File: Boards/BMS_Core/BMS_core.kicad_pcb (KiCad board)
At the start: 2 copper layers, 73.7 x 61 mm, 72 parts, among them IC1 ATMEGA16M1, J1 CONN_02X03, J2 B5B-PH-K-S, J3 MM_F_VT_20, J4 MicroFit_V_2, J5 isoSPI-Cutout, K1 G5Q-1A4-DC5-5V, Q1 SSM3K333R, T1 T_LAN_7490100111A, U1 MCP2561-E_SN, U101 TPS561201, U2 SN74LVC1G17, U3 LTC6820HMS, U4 MCP6001, U5 MCP6001, U6 MCP6001, U7 SN74LVC1G32, Y1 Crystal_SMD

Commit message: update BMS Core schemtic)
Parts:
- moved C6 71.3 mm to (115.9, 32.4), turned to 0 degrees
- moved T1 70.1 mm to (68.0, 41.0), turned to 0 degrees
- moved C9 69.1 mm to (108.4, 37.4), turned to 0 degrees
- moved R11 65.0 mm to (114.2, 42.2)
- moved C8 62.0 mm to (101.6, 45.8), turned to 0 degrees
- moved R3 59.2 mm to (105.9, 43.1), turned to 0 degrees
- moved U3 57.3 mm to (102.5, 38.8), turned to 0 degrees
- moved R8 56.8 mm to (110.1, 45.9), turned to 0 degrees
- moved R9 54.6 mm to (105.2, 48.8), turned to 0 degrees
- moved R10 54.1 mm to (102.2, 53.2), turned to 0 degrees
- moved U2 51.9 mm to (96.9, 43.9)
- moved J4 50.4 mm to (94.2, 37.6)
- moved Y1 47.9 mm to (111.3, 28.5)
- moved C1 46.9 mm to (113.0, 36.4)
- moved C10 46.6 mm to (120.8, 27.7)
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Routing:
- net VCC: track 240.5 -> 20.5 mm, vias 7 -> 1
- net /VOUT: track 81.1 -> 0.00 mm, vias 2 -> 0
- net /BSPD_CURRENT: track 79.8 -> 0.00 mm, vias 4 -> 0
- net /MISO: track 73.4 -> 0.00 mm, vias 3 -> 0
- net /VREF: track 72.7 -> 0.00 mm, vias 6 -> 0
- net /RESET: track 70.9 -> 0.00 mm, vias 4 -> 0
- net /MOSI: track 69.8 -> 0.00 mm, vias 3 -> 0
- net /SCK: track 64.6 -> 0.00 mm, vias 5 -> 0
- net GND: track 68.3 -> 14.4 mm, vias 46 -> 14
- net /RXCAN: track 42.6 -> 0.00 mm
- net /BMS_SENSE: track 40.0 -> 0.00 mm, vias 2 -> 0
- net /~OCD: track 39.7 -> 0.00 mm, vias 2 -> 0
- net +12V: track 55.5 -> 17.0 mm
- net /RJ45_LED2: track 37.1 -> 0.00 mm, vias 2 -> 0
- net /FAN_PWM_RAW: track 35.6 -> 2.57 mm, vias 2 -> 0
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- removed copper zone on B.Cu, net GND
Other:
- board outline removed
- board text removed: "GLV"
- board text removed: "HV"
- board text removed: "IM IP"
- board text removed: "MKIV BMS Core Rev 1.4 Olin Electric Motorsports Alexander Hoppe '19 Lucky Jordan '21 5/19/19"
- board text removed: "PD5"
- board text removed: "PD6"
- board text removed: "PD7"

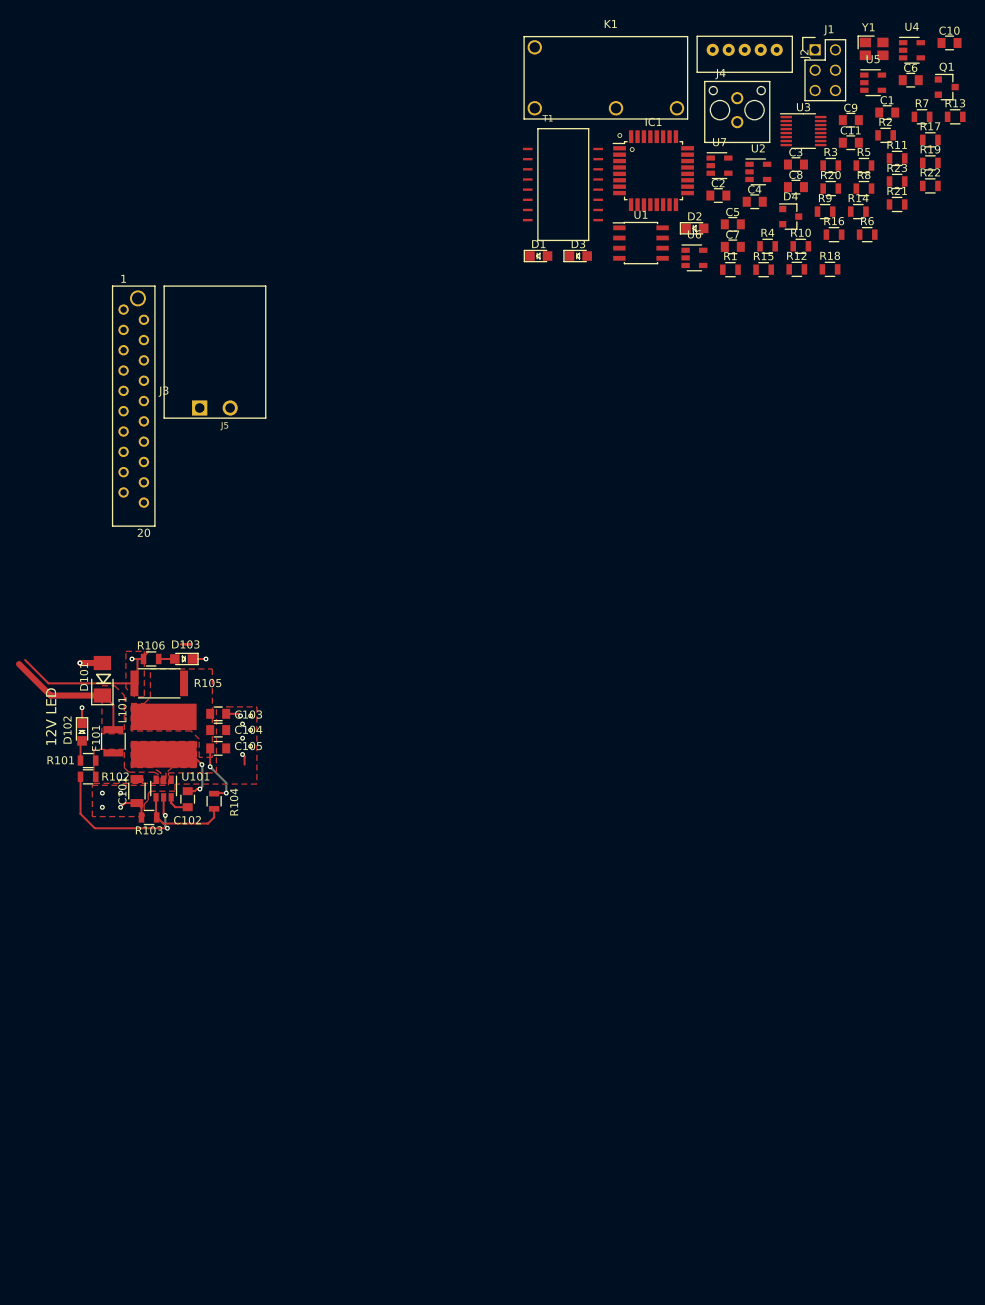
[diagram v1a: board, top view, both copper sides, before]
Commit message: Added bypass cap to Logic block; new core layout for ss layout
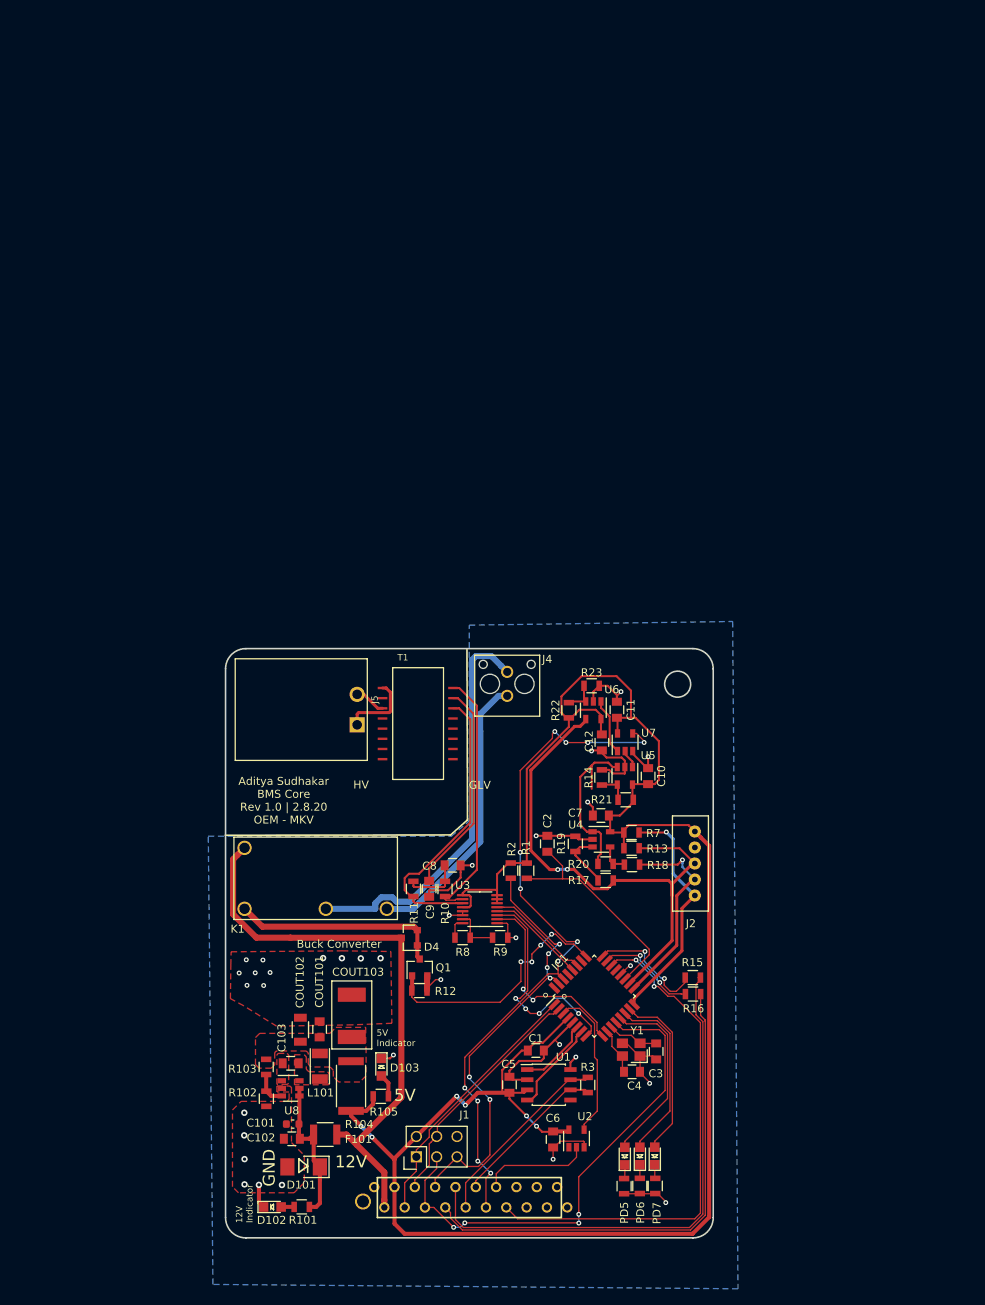
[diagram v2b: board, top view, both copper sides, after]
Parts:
- removed C104: C_1uF, footprints:C_0805_OEM
- removed C105: C_0.1uF, footprints:C_0805_OEM
- removed D1, D2, D3: LED_0805, footprints:LED_0805_OEM
- removed R106: R_200, footprints:R_0805_OEM
- removed U101: TPS561201, footprints:SOT-23-6_OEM
- added C12: C_0.1uF, footprints:C_0805_OEM, F.Cu at (77.3, 115.2)
- added COUT101: C_47uF, footprints:C_0805_OEM, F.Cu at (42.0, 151.0)
- added COUT102: C_22uF, footprints:C_1206_OEM, F.Cu at (39.6, 151.1)
- added COUT103: C_33uF, footprints:Fuse_1812, F.Cu at (46.0, 152.0)
- added PD5: LED_0805, footprints:LED_0805_OEM, F.Cu at (80.2, 166.9)
- added PD6: LED_0805, footprints:LED_0805_OEM, F.Cu at (82.0, 166.9)
- added PD7: LED_0805, footprints:LED_0805_OEM, F.Cu at (83.9, 166.9)
- added U8: TPS560430YF, footprints:SOT-23-6_OEM, F.Cu at (38.4, 158.4)
- C101: value C_22uF -> C_2.2uF; footprint footprints:C_1206_OEM -> footprints:C_0603_1608Metric
- C103: value C_47uF -> C_0.1uF
- J3: moved to B.Cu
- L101: value L_4.7uH -> L_100uH; footprint footprints:4.7uH_Inductor_OEM -> footprints:L_100uH_OEM
- R102: value R_10K -> R_25K
- R103: value R_10K -> R_100K
- R104: value R_54.9K -> R_0_2512; footprint footprints:R_0805_OEM -> footprints:R_2512_OEM
- R105: value R_0_2512 -> R_200; footprint footprints:R_2512_OEM -> footprints:R_0805_OEM
- moved J1 147.1 mm to (54.1, 167.0), turned to 90 degrees
- moved C6 139.8 mm to (71.2, 164.8), turned to 90 degrees
- moved R5 130.6 mm to (82.0, 170.6), turned to 270 degrees
- moved Y1 128.7 mm to (81.0, 153.6), turned to 180 degrees
- moved Q1 128.3 mm to (54.5, 143.3), turned to 90 degrees
- moved C1 125.2 mm to (69.0, 153.7)
- moved U2 122.9 mm to (74.1, 164.7), turned to 90 degrees
- moved R6 121.8 mm to (84.0, 170.6), turned to 270 degrees
- moved R3 118.9 mm to (75.5, 158.0), turned to 270 degrees
- moved R4 118.8 mm to (80.1, 170.6), turned to 270 degrees
- moved C3 112.2 mm to (84.1, 153.8), turned to 270 degrees
- moved C5 111.1 mm to (65.7, 158.0), turned to 90 degrees
- moved J3 110.8 mm to (53.9, 170.8), turned to 270 degrees
- moved C4 109.8 mm to (81.1, 156.3)
- moved C9 109.6 mm to (55.7, 133.5), turned to 270 degrees
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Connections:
- C102 pad 1: Net-(C102-Pad1) -> Net-(C101-Pad1)
- C102 pad 2: Net-(C102-Pad2) -> GND
- C103 pad 2: GND -> Net-(C103-Pad2)
- D101 pad 1: +12V -> Net-(C101-Pad1)
- D4 pad 2: (no net) -> Net-(D4-Pad1)
- J3 pad 15: /Charge-Enable-1 -> GND
- J3 pad 16: /Charge-Enable-2 -> GND
- J3 pad 21: (no net) -> GND
- L101 pad 1: Net-(C102-Pad2) -> Net-(C103-Pad1)
- L101 pad 2: Net-(C103-Pad1) -> Net-(COUT101-Pad1)
- R102 pad 2: Net-(C101-Pad1) -> GND
- R103 pad 1: Net-(R103-Pad1) -> Net-(R102-Pad1)
- R103 pad 2: GND -> Net-(COUT101-Pad1)
- R104 pad 1: Net-(R103-Pad1) -> VCC
- R104 pad 2: Net-(C103-Pad1) -> Net-(COUT101-Pad1)
- R105 pad 2: Net-(C103-Pad1) -> Net-(D103-Pad2)
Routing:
- net VCC: track 20.5 -> 254.8 mm, vias 1 -> 6
- net /BSPD_CURRENT: track 0.00 -> 88.9 mm, vias 0 -> 12
- net GND: track 14.4 -> 93.7 mm, vias 14 -> 28
- net /VOUT: track 0.00 -> 67.9 mm, vias 0 -> 2
- net /RJ45_LED2: track 0.00 -> 66.6 mm
- net /BMS_SENSE: track 0.00 -> 64.2 mm, vias 0 -> 2
- net /RJ45_LED1: track 0.00 -> 63.2 mm
- net /SCK: track 0.00 -> 62.2 mm, vias 0 -> 4
- net /RESET: track 0.00 -> 57.3 mm, vias 0 -> 6
- net +12V: track 17.0 -> 71.6 mm
- net /SHDN_OUT(BMS->IMD): track 0.00 -> 50.6 mm
- net Net-(R11-Pad2): track 0.00 -> 36.5 mm
- net /SHDN_IN(MAIN_PACK->BMS): track 0.00 -> 35.5 mm
- net /MISO: track 0.00 -> 33.1 mm
- net Net-(R10-Pad1): track 0.00 -> 32.4 mm
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- added copper zone on B.Cu, net GND
- added copper zone on F.Cu, net Net-(C103-Pad2)
- added copper zone on F.Cu, net Net-(COUT101-Pad1)
- removed copper zone on F.Cu, net +12V
- removed copper zone on F.Cu, net Net-(C101-Pad1)
- removed copper zone on F.Cu, net Net-(C102-Pad2)
- removed copper zone on F.Cu, net VCC
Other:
- board outline added: 61 x 73.7 mm
- board text added: "12V"
- board text added: "12V Indicator"
- board text added: "5V"
- board text added: "5V Indicator"
- board text added: "Aditya Sudhakar BMS Core Rev 1.0 | 2.8.20 OEM - MKV"
- board text added: "Buck Converter"
- board text added: "GLV"
- board text added: "GND"
- board text added: "HV"
- board text removed: "12V LED"

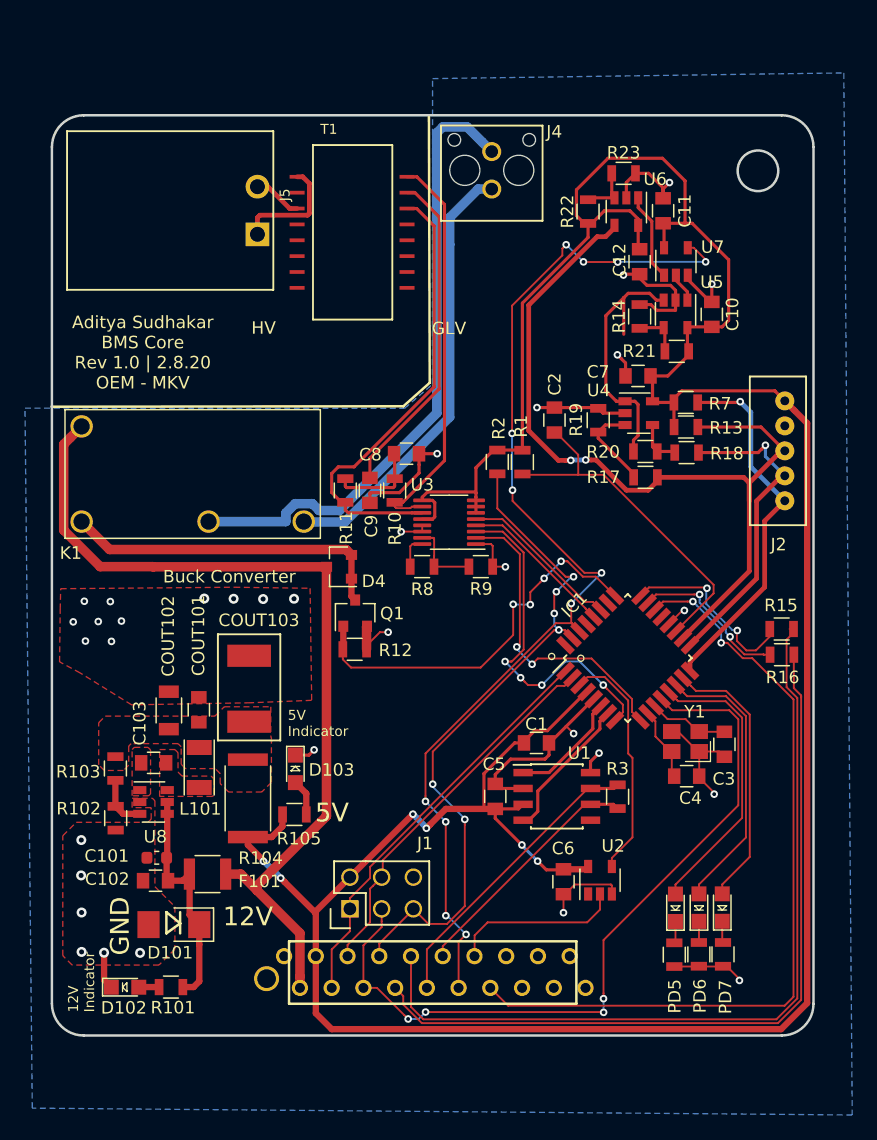
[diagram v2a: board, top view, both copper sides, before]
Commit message: new transformer, mounting hole, moved I sensor
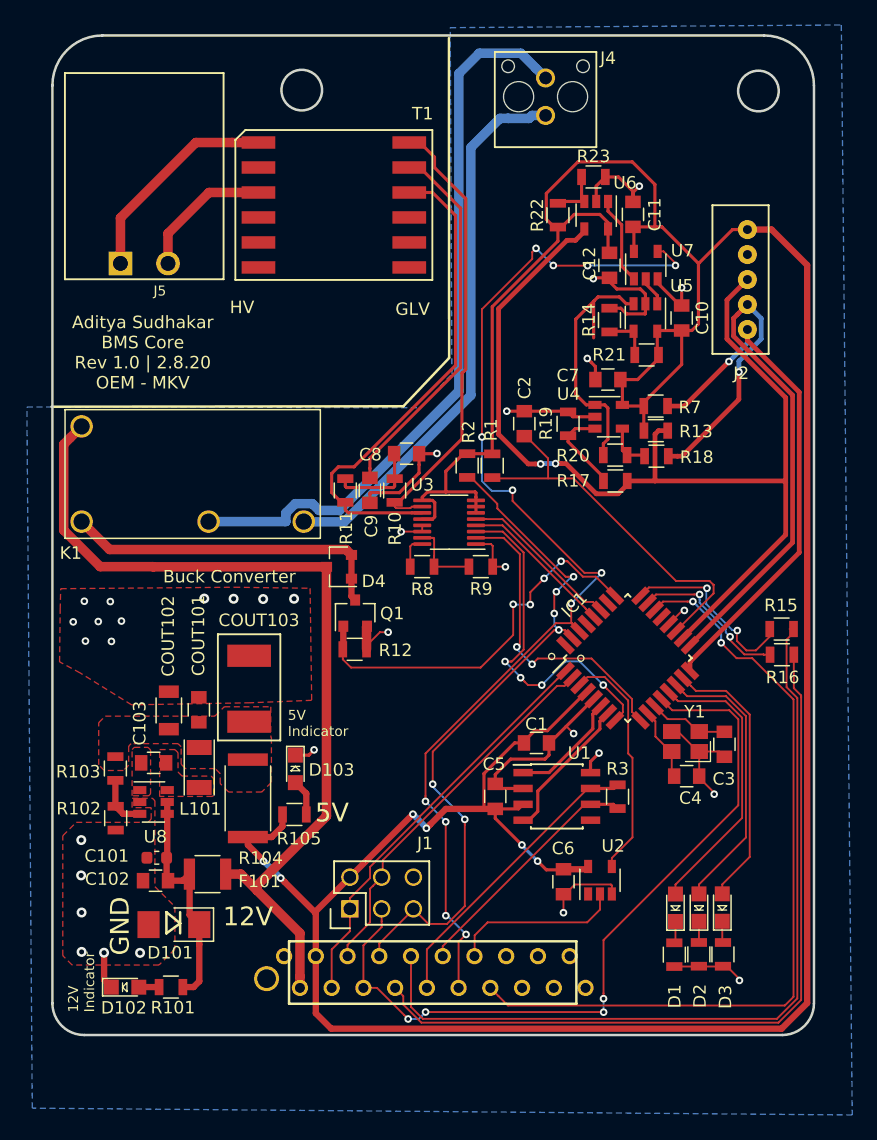
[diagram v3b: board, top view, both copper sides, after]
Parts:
- T1: value T_LAN_7490100111A -> T_LAN_SM91501ALE; footprint footprints:T_LAN_7490100111A -> footprints:T_LAN_SM91501ALE
- moved J2 14.0 mm to (85.9, 116.6)
- moved J5 10.0 mm to (37.6, 115.3), turned to 0 degrees
- moved J4 7.30 mm to (69.8, 103.5)
- moved T1 3.71 mm to (52.8, 110.6), turned to 270 degrees
- moved C11 2.43 mm to (76.8, 111.4)
- moved C2 2.43 mm to (68.1, 128.1)
- moved R13 2.43 mm to (78.6, 128.7)
- moved R19 2.43 mm to (71.6, 128.1)
- moved R2 2.43 mm to (63.5, 131.5)
- moved C10 2.43 mm to (80.7, 119.7)
- moved C7 2.43 mm to (74.8, 124.6)
- moved R23 2.43 mm to (73.6, 108.4)
- moved U5 2.43 mm to (77.8, 119.6)
- moved U7 2.43 mm to (77.8, 115.4)
- moved C12 2.43 mm to (74.9, 115.5)
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- renumbered PD5 to D1, PD6 to D2, PD7 to D3
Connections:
- T1 pad 10: Net-(T1-Pad10) -> Net-(R11-Pad2)
- T1 pad 11: Net-(T1-Pad11) -> Net-(C9-Pad1)
- T1 pad 12: (no net) -> Net-(R10-Pad1)
- T1 pad 4: (no net) -> Net-(T1-Pad4)
- T1 pad 5: (no net) -> Net-(T1-Pad5)
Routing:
- net /VREF: track 25.5 -> 49.4 mm
- net VCC: track 254.8 -> 273.1 mm
- net /VOUT: track 67.9 -> 85.0 mm
- net /~OCD: track 29.6 -> 42.2 mm
- net /SHDN_IN(MAIN_PACK->BMS): track 35.5 -> 44.5 mm
- net /SHDN_OUT(BMS->IMD): track 50.6 -> 59.1 mm
- net Net-(J5-Pad1): track 9.23 -> 17.2 mm
- net Net-(J5-Pad2): track 3.90 -> 11.0 mm
- net Net-(R10-Pad1): track 32.4 -> 36.3 mm
- net Net-(R11-Pad2): track 36.5 -> 40.4 mm
- net Net-(C9-Pad1): track 26.6 -> 30.0 mm
- net Net-(C2-Pad1): track 28.2 -> 30.5 mm
- net /BSPD_CURRENT: track 88.9 -> 90.7 mm
- net /RESET: track 57.3 -> 58.2 mm
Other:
- board size 61 x 73.7 mm -> 61 x 80 mm

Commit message: BMS core changes
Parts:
- added 12V: Test_Point_SMD, footprints:Test_Point_SMD, F.Cu at (55.4, 149.9)
- added BSPD: Test_Point_SMD, footprints:Test_Point_SMD, F.Cu at (80.2, 101.6)
- added C13: C_0.1uF, footprints:C_0805_OEM, F.Cu at (58.2, 140.4)
- added GND: Test_Point_SMD, footprints:Test_Point_SMD, F.Cu at (55.5, 153.4)
- added IM: Test_Point_SMD, footprints:Test_Point_SMD, F.Cu at (35.4, 116.9)
- added IP: Test_Point_SMD, footprints:Test_Point_SMD, F.Cu at (41.7, 116.9)
- K1: value G5Q-1A4-DC5-5V -> G5Q-1A4-DC12
- R8: value R_3.01K -> R_1K
- moved C2 15.3 mm to (79.0, 138.8)
- moved R2 11.5 mm to (73.4, 137.4)
- moved R1 11.4 mm to (75.3, 137.4)
- moved J1 2.99 mm to (53.3, 164.1)
- moved K1 2.42 mm to (32.7, 138.4)
- moved J5 1.63 mm to (38.0, 113.7)
- moved R8 1.44 mm to (61.3, 139.6)
- moved D4 0.54 mm to (53.8, 139.6)
- renumbered D1 to PD5, D2 to PD6, D3 to PD7
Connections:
- net Net-(J5-Pad1) renamed /IM
- net Net-(J5-Pad2) renamed /IP
- IC1 pad 29: Net-(IC1-Pad29) -> /CHARGE_ENABLE1
- J3 pad 19: GND -> /CHARGE_ENABLE1
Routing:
- net /CHARGE_ENABLE1: track 0.00 -> 51.9 mm, vias 0 -> 5
- net VCC: track 273.1 -> 294.6 mm
- net Net-(C2-Pad1): track 30.5 -> 15.8 mm
- net /BSPD_CURRENT: track 90.7 -> 102.1 mm, vias 12 -> 15
- net GND: track 93.7 -> 103.6 mm, vias 28 -> 30
- net /RESET: track 58.2 -> 54.6 mm
- net +12V: track 71.6 -> 74.6 mm
- net /IP: track 11.0 -> 13.8 mm
- net /SCK: track 62.1 -> 64.7 mm
- net /MISO: track 33.1 -> 35.1 mm
- net /IM: track 17.2 -> 18.8 mm
- net /RELAY_DRIVE: track 31.4 -> 33.1 mm
- net /SHDN_IN(MAIN_PACK->BMS): track 44.5 -> 45.8 mm
- net /MOSI: track 30.3 -> 31.5 mm
- net Net-(R8-Pad2): track 6.03 -> 5.18 mm
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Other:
- outline, holes or cut-outs redrawn
- board text added: "5V LED"
- board text added: "Aditya Sudhakar BMS Core Rev 1.0 | 2.10.20 OEM - MKV"
- board text added: "IM"
- board text added: "IP"
- board text added: "OUT"
- board text added: "VCC GND VOUT VREF OCD"
- board text removed: "5V Indicator"
- board text removed: "Aditya Sudhakar BMS Core Rev 1.0 | 2.8.20 OEM - MKV"
